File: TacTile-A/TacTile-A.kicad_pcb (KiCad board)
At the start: 2 copper layers, 59.9 x 59.9 mm, 100 parts, among them J1 Conn_01x01, J2 Conn_01x01, J3 Conn_01x01, J4 Conn_01x01, U1 MCP14A0304xMNY, U10 MCP14A0304xMNY, U11 MCP14A0304xMNY, U12 MCP14A0304xMNY, U13 MCP14A0304xMNY, U14 MCP14A0304xMNY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

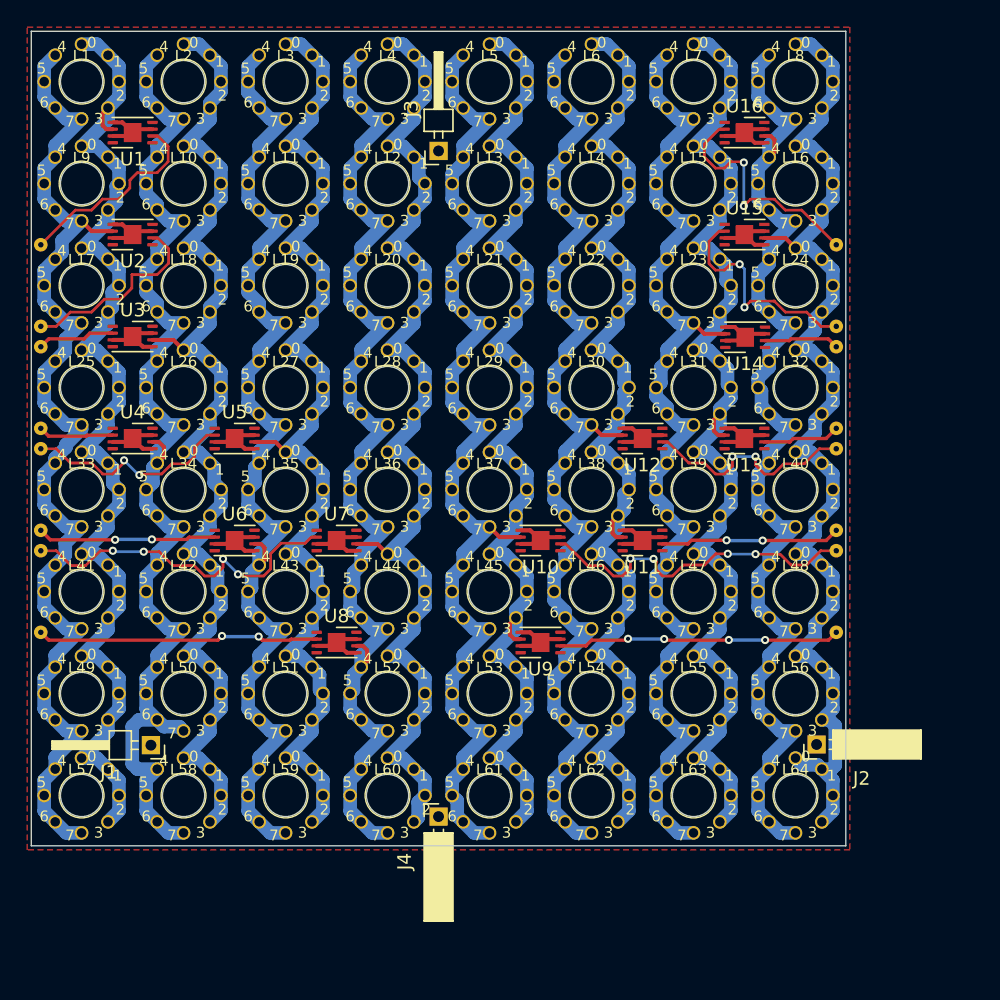
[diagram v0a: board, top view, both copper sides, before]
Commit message: Added photoresistor footprint and enlarged main boards to 60mm
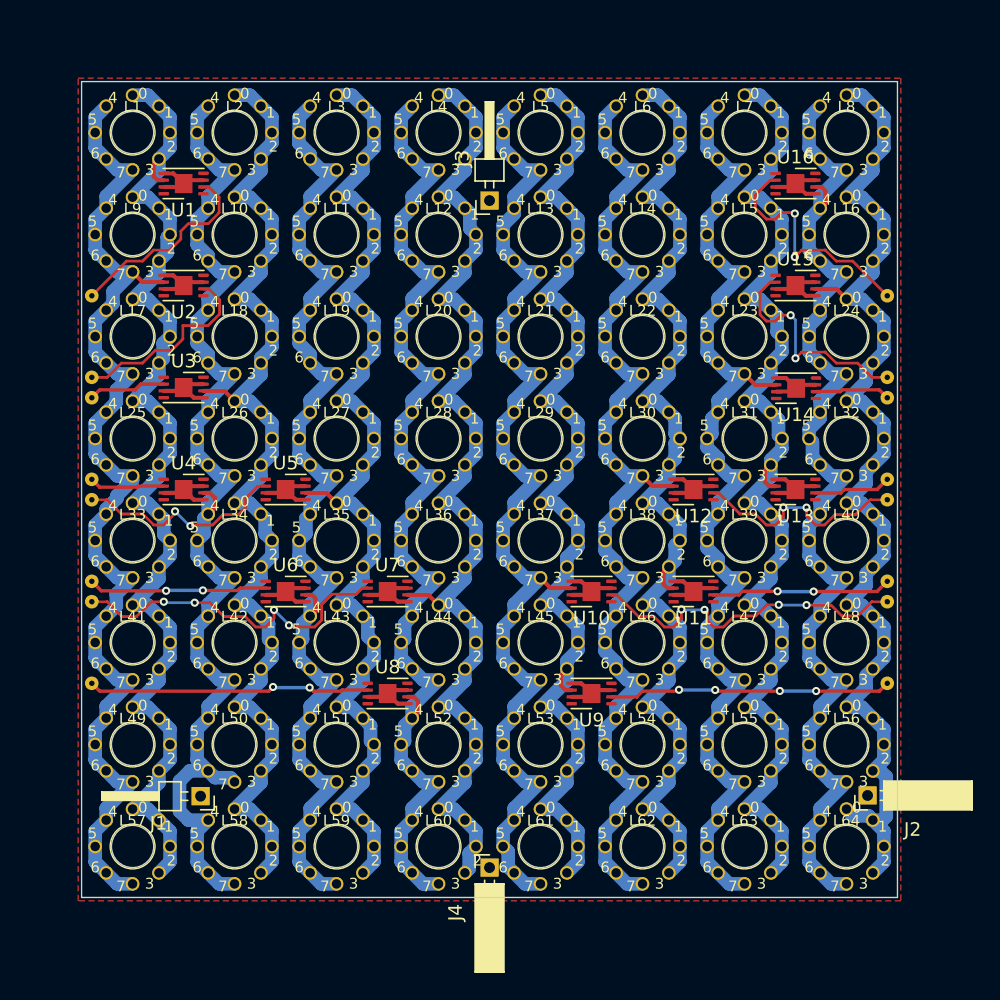
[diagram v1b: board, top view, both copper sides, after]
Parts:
- moved J2 5.30 mm to (82.8, 77.5)
- moved J4 5.30 mm to (55.0, 82.8)
- moved JMP1 5.30 mm to (25.8, 40.8)
- moved JMP10 5.30 mm to (84.2, 63.2)
- moved JMP11 5.30 mm to (84.2, 61.8)
- moved JMP12 5.30 mm to (84.2, 55.8)
- moved JMP13 5.30 mm to (84.2, 54.2)
- moved JMP14 5.30 mm to (84.2, 48.2)
- moved JMP15 5.30 mm to (84.2, 46.8)
- moved JMP16 5.30 mm to (84.2, 40.8)
- moved JMP2 5.30 mm to (25.8, 46.8)
- moved JMP3 5.30 mm to (25.8, 48.2)
- moved JMP4 5.30 mm to (25.8, 54.2)
- moved JMP5 5.30 mm to (25.8, 55.8)
- moved JMP6 5.30 mm to (25.8, 61.8)
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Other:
- board size 59.9 x 59.9 mm -> 60 x 60 mm

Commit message: Swapped headers and sockets on board A
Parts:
- J1, J3: footprint Connector_PinHeader_2.00mm:PinHeader_1x01_P2.00mm_Horizontal -> Connector_PinSocket_2.00mm:PinSocket_1x01_P2.00mm_Horizontal
- J2, J4: footprint Connector_PinSocket_2.00mm:PinSocket_1x01_P2.00mm_Horizontal -> Connector_PinHeader_2.00mm:PinHeader_1x01_P2.00mm_Horizontal
- turned J1 to 0 degrees
- turned J2 to 0 degrees
- turned J3 to -90 degrees
- turned J4 to -90 degrees

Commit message: Enlarged grounding pins on board A
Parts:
- J1, J3: footprint Connector_PinSocket_2.00mm:PinSocket_1x01_P2.00mm_Horizontal -> Connector_PinSocket_2.54mm:PinSocket_1x01_P2.54mm_Horizontal
- J2, J4: footprint Connector_PinHeader_2.00mm:PinHeader_1x01_P2.00mm_Horizontal -> Connector_PinHeader_2.54mm:PinHeader_1x01_P2.54mm_Horizontal
- moved J2 4.80 mm to (78.0, 77.5)
- moved J4 4.80 mm to (55.0, 78.0)
- moved J1 1.45 mm to (32.3, 77.5)
- moved J3 1.45 mm to (55.0, 32.3)
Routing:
- net /GND4: track 85.7 -> 82.3 mm
- net /GND15: track 84.1 -> 82.5 mm
